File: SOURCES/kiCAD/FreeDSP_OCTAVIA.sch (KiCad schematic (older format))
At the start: 167 parts, among them IC1 TPS5430DDA, J13 Conn_01x05, J2 DC7.5V-9V IN, J4 Header_01x06, J7 Header_01x04, J8 Header_01x04, P1 Conn_02x20_Odd_Even, Q1 AO3401A, Q2 MMBT5401, Q3 2N7002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

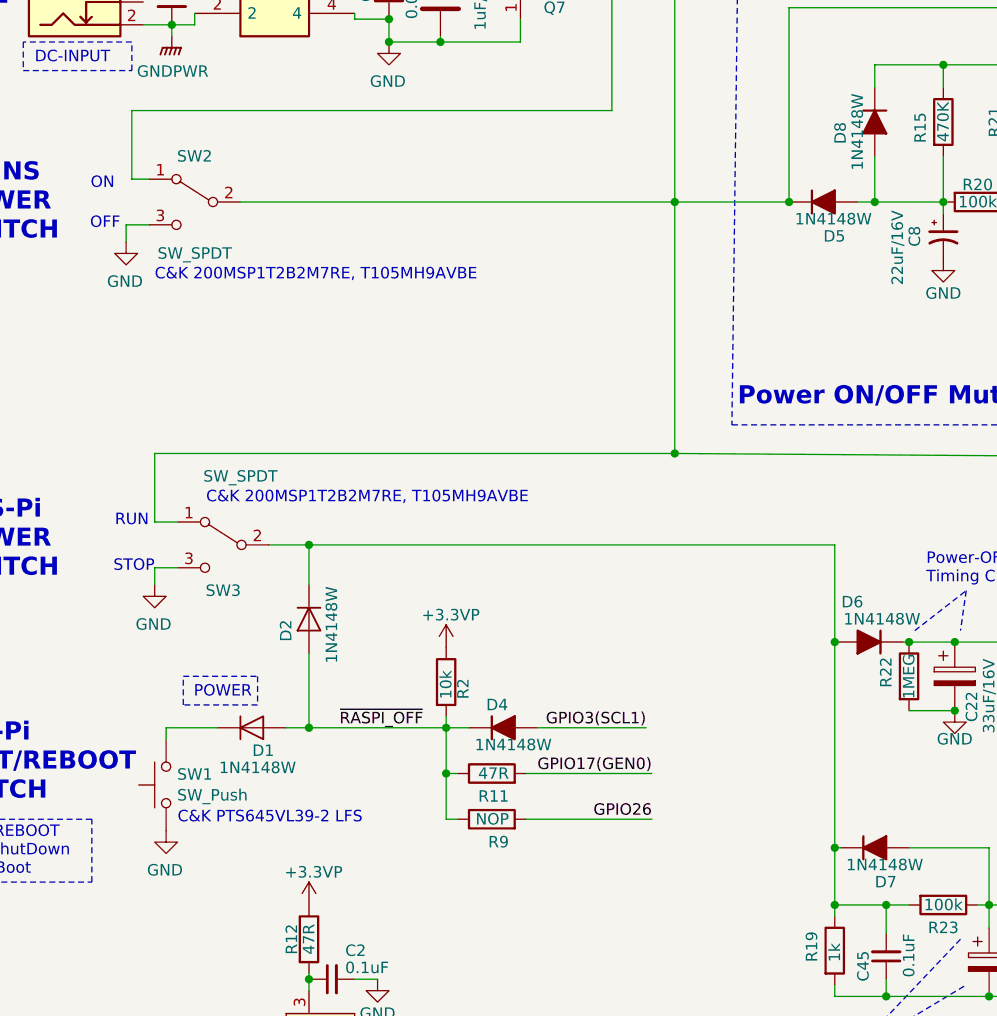
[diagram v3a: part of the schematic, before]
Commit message: A method of board type convertion had changed.
Add an AGND fill on the bottom layer. The connection path for the Standard type board had changed. No features/functions changed.
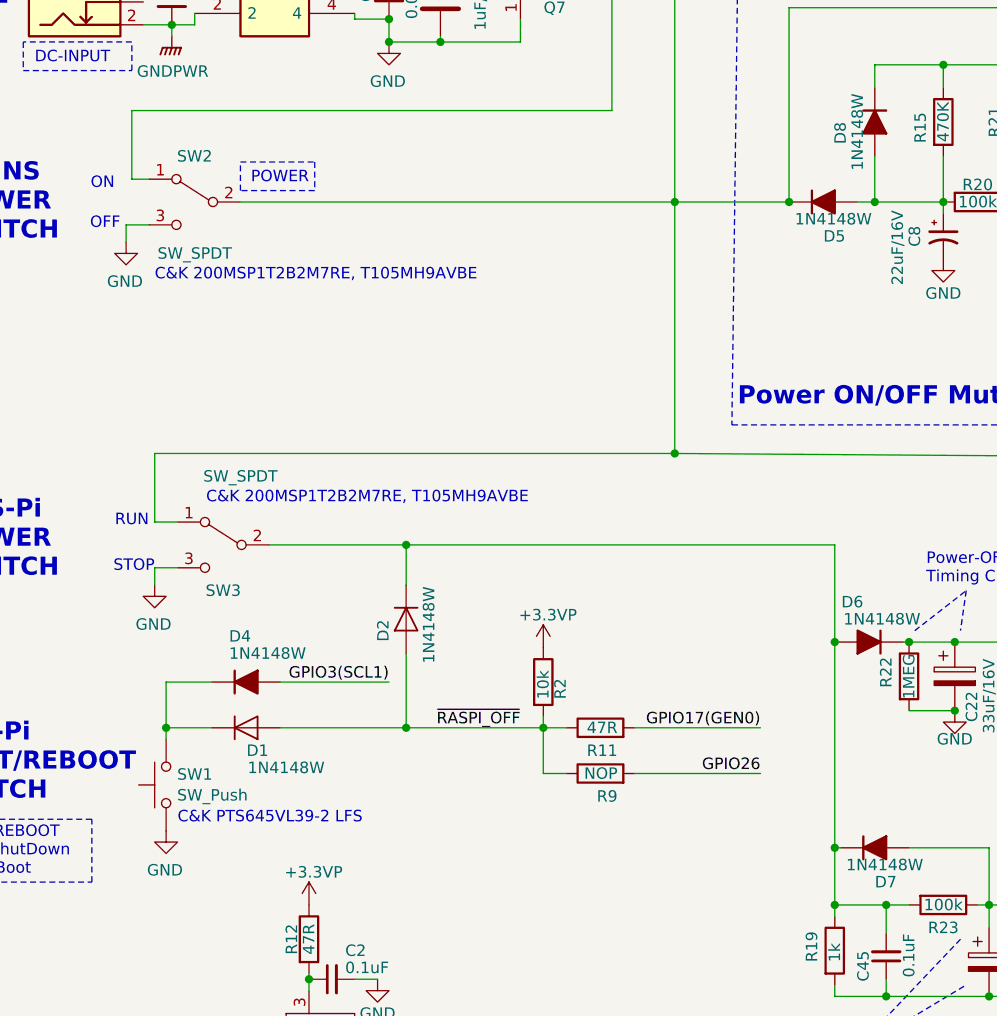
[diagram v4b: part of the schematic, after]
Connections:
- net ~RASPI_OFF: no longer D4.1 (K)
- net at D1.1 (K), SW1.2: now also D4.1 (K)
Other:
- moved on the sheet: D1, D2, D4, R11, R2, R9
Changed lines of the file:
@@
 Sheet 1 3
 Title "FreeDSP OVTAVIA Main Board"
-Date "2023-12-03"
-Rev "1.1"
+Date "2024-01-03"
+Rev "1.2"
 Comp ""
 Comment1 ""
@@
 Text Notes 2100 2375 2    50   ~ 0
 OFF
-Text Notes 2675 4425 2    50   ~ 0
+Text Notes 2925 2175 2    50   ~ 0
 POWER
 Wire Notes Line
-	2700 4325 2700 4450
+	2950 2075 2950 2200
 Wire Notes Line
-	2700 4450 2375 4450
+	2950 2200 2625 2200
 Wire Notes Line
-	2375 4450 2375 4325
+	2625 2200 2625 2075
 Wire Notes Line
-	2375 4325 2700 4325
+	2625 2075 2950 2075
 $Comp
 L Device:C_Small C?
@@
 L MW-ADAU1466BB-rescue:D-CS5368TDM-rescue-RasPiAudioHat-rescue D2
 U 1 1 5E32A9DB
-P 2925 4075
-F 0 "D2" H 2975 4175 50  0000 C CNN
-F 1 "1N4148W" H 2950 3975 50  0000 C CNN
-F 2 "Diode_SMD:D_SOD-123" H 2925 4075 50  0001 C CNN
-F 3 "" H 2925 4075 50  0001 C CNN
-F 4 "C81598 " H 2925 4075 50  0001 C CNN "JLPCB#"
-F 5 "Si Switching Diode" H 2925 4075 50  0001 C CNN "Description"
-	1    2925 4075
+P 3350 4075
+F 0 "D2" H 3400 4175 50  0000 C CNN
+F 1 "1N4148W" H 3375 3975 50  0000 C CNN
+F 2 "Diode_SMD:D_SOD-123" H 3350 4075 50  0001 C CNN
+F 3 "" H 3350 4075 50  0001 C CNN
+F 4 "C81598 " H 3350 4075 50  0001 C CNN "JLPCB#"
+F 5 "Si Switching Diode" H 3350 4075 50  0001 C CNN "Description"
+	1    3350 4075
 	0    -1   1    0
 $EndComp
-Text Label 3425 4550 2    50   ~ 0
+Text Label 3850 4550 2    50   ~ 0
 ~RASPI_OFF
 $Comp
 L MW-ADAU1466BB-rescue:D-CS5368TDM-rescue-RasPiAudioHat-rescue D1
 U 1 1 5E34C8F1
-P 2675 4550
-F 0 "D1" H 2725 4650 50  0000 C CNN
-F 1 "1N4148W" H 2700 4725 50  0000 C CNN
-F 2 "Diode_SMD:D_SOD-123" H 2675 4550 50  0001 C CNN
-F 3 "" H 2675 4550 50  0001 C CNN
-F 4 "C81598 " H 2675 4550 50  0001 C CNN "JLPCB#"
-F 5 "Si Switching Diode" H 2675 4550 50  0001 C CNN "Description"
-	1    2675 4550
+P 2650 4550
+F 0 "D1" H 2700 4650 50  0000 C CNN
+F 1 "1N4148W" H 2825 4725 50  0000 C CNN
+F 2 "Diode_SMD:D_SOD-123" H 2650 4550 50  0001 C CNN
+F 3 "" H 2650 4550 50  0001 C CNN
+F 4 "C81598 " H 2650 4550 50  0001 C CNN "JLPCB#"
+F 5 "Si Switching Diode" H 2650 4550 50  0001 C CNN "Description"
+	1    2650 4550
 	1    0    0    1
 $EndComp
@@
 RAS-Pi\nSHUT/REBOOT\nSWITCH
 Wire Wire Line
-	2300 4550 2525 4550
+	2300 4550 2500 4550
 $Comp
 L MW-ADAU1466BB-rescue:R-CS5368TDM-rescue-RasPiAudioHat-rescue R13
@@
 L Device:R R?
 U 1 1 5DF72E64
-P 3725 4750
+P 4200 4550
 AR Path="/5DEF3C17/5DF72E64" Ref="R?"  Part="1"
 AR Path="/5DF72E64" Ref="R11"  Part="1"
-F 0 "R11" V 3625 4675 50  0000 L CNN
-F 1 "47R" V 3725 4675 50  0000 L CNN
-F 2 "Resistor_SMD:R_0805_2012Metric_Pad1.20x1.40mm_HandSolder" V 3655 4750 50  0001 C CNN
-F 3 "~" H 3725 4750 50  0001 C CNN
-F 4 "C17714" H 3725 4750 50  0001 C CNN "JLPCB#"
-	1    3725 4750
+F 0 "R11" V 4100 4475 50  0000 L CNN
+F 1 "47R" V 4200 4475 50  0000 L CNN
+F 2 "Resistor_SMD:R_0805_2012Metric_Pad1.20x1.40mm_HandSolder" V 4130 4550 50  0001 C CNN
+F 3 "~" H 4200 4550 50  0001 C CNN
+F 4 "C17714" H 4200 4550 50  0001 C CNN "JLPCB#"
+	1    4200 4550
 	0    -1   -1   0
 $EndComp
-Text Label 4425 4950 2    50   ~ 0
+Text Label 4900 4750 2    50   ~ 0
 GPIO26
 Wire Wire Line
-	3875 4950 4425 4950
-Wire Wire Line
-	3525 4950 3525 4750
-Text Label 4425 4750 2    50   ~ 0
+	4350 4750 4900 4750
+Text Label 4900 4550 2    50   ~ 0
 GPIO17(GEN0)
 $Comp
 L Device:R R?
 U 1 1 5DF72E6F
-P 3725 4950
+P 4200 4750
 AR Path="/5DEF3C17/5DF72E6F" Ref="R?"  Part="1"
 AR Path="/5DF72E6F" Ref="R9"  Part="1"
-F 0 "R9" V 3625 4875 50  0000 L CNN
-F 1 "NOP" V 3725 4875 50  0000 L CNN
-F 2 "Resistor_SMD:R_0805_2012Metric_Pad1.20x1.40mm_HandSolder" V 3655 4950 50  0001 C CNN
-F 3 "~" H 3725 4950 50  0001 C CNN
-F 4 "NOP" H 3725 4950 50  0001 C CNN "JLPCB#"
-F 5 "Selectable Exclusive Mount Jumper R" H 3725 4950 50  0001 C CNN "Description"
-	1    3725 4950
+F 0 "R9" V 4100 4675 50  0000 L CNN
+F 1 "NOP" V 4200 4675 50  0000 L CNN
+F 2 "Resistor_SMD:R_0805_2012Metric_Pad1.20x1.40mm_HandSolder" V 4130 4750 50  0001 C CNN
+F 3 "~" H 4200 4750 50  0001 C CNN
+F 4 "NOP" H 4200 4750 50  0001 C CNN "JLPCB#"
+F 5 "Selectable Exclusive Mount Jumper R" H 4200 4750 50  0001 C CNN "Description"
+	1    4200 4750
 	0    -1   -1   0
 $EndComp
-Connection ~ 3525 4750
 Wire Wire Line
-	3875 4750 4425 4750
+	4350 4550 4900 4550
 $Comp
 L Device:D_ALT D?
 U 1 1 5DF72E77
-P 3775 4550
+P 2650 4350
 AR Path="/5D60B524/5DF72E77" Ref="D?"  Part="1"
 AR Path="/5DF72E77" Ref="D4"  Part="1"
 AR Path="/5DEF3C17/5DF72E77" Ref="D?"  Part="1"
-F 0 "D4" H 3700 4650 50  0000 L CNN
-F 1 "1N4148W" H 3650 4475 50  0000 L CNN
-F 2 "Diode_SMD:D_SOD-123" H 3775 4550 50  0001 C CNN
-F 3 "~" H 3775 4550 50  0001 C CNN
-F 4 "C81598 " H 3775 4550 50  0001 C CNN "JLPCB#"
-F 5 "Si Switching Diode" H 3775 4550 50  0001 C CNN "Description"
-	1    3775 4550
+F 0 "D4" H 2575 4550 50  0000 L CNN
+F 1 "1N4148W" H 2575 4475 50  0000 L CNN
+F 2 "Diode_SMD:D_SOD-123" H 2650 4350 50  0001 C CNN
+F 3 "~" H 2650 4350 50  0001 C CNN
+F 4 "C81598 " H 2650 4350 50  0001 C CNN "JLPCB#"
+F 5 "Si Switching Diode" H 2650 4350 50  0001 C CNN "Description"
+	1    2650 4350
 	1    0    0    -1
 $EndComp
 Wire Wire Line
-	3525 4550 3525 4750
+	3950 4550 3950 4750
 Wire Wire Line
-	3925 4550 4400 4550
-Text Label 4400 4550 2    50   ~ 0
+	2800 4350 3275 4350
+Text Label 3275 4350 2    50   ~ 0
 GPIO3(SCL1)
 $Comp
 L Device:R R?
 U 1 1 5DF72E80
-P 3525 4350
+P 3950 4350
 AR Path="/5DEF3C17/5DF72E80" Ref="R?"  Part="1"
 AR Path="/5DF72E80" Ref="R2"  Part="1"
-F 0 "R2" V 3600 4275 50  0000 L CNN
-F 1 "10k" V 3525 4275 50  0000 L CNN
-F 2 "Resistor_SMD:R_0805_2012Metric_Pad1.20x1.40mm_HandSolder" V 3455 4350 50  0001 C CNN
-F 3 "~" H 3525 4350 50  0001 C CNN
-F 4 "C17414" H 3525 4350 50  0001 C CNN "JLPCB#"
-	1    3525 4350
+F 0 "R2" V 4025 4275 50  0000 L CNN
+F 1 "10k" V 3950 4275 50  0000 L CNN
+F 2 "Resistor_SMD:R_0805_2012Metric_Pad1.20x1.40mm_HandSolder" V 3880 4350 50  0001 C CNN
+F 3 "~" H 3950 4350 50  0001 C CNN
+F 4 "C17414" H 3950 4350 50  0001 C CNN "JLPCB#"
+	1    3950 4350
 	1    0    0    -1
 $EndComp
 Wire Wire Line
-	3525 4500 3525 4550
-Connection ~ 3525 4550
-Wire Wire Line
-	3525 4550 3625 4550
-Wire Wire Line
-	3575 4750 3525 4750
+	3950 4500 3950 4550
+Connection ~ 3950 4550
 Wire Wire Line
-	3575 4950 3525 4950
+	3950 4550 4050 4550
 Wire Notes Line style solid
 	1975 5225 1975 4950
@@
 L power:+3.3VP #PWR09
 U 1 1 6069E068
-P 3525 4200
-F 0 "#PWR09" H 3675 4150 50  0001 C CNN
-F 1 "+3.3VP" H 3545 4343 50  0000 C CNN
-F 2 "" H 3525 4200 50  0001 C CNN
-F 3 "" H 3525 4200 50  0001 C CNN
-	1    3525 4200
+P 3950 4200
+F 0 "#PWR09" H 4100 4150 50  0001 C CNN
+F 1 "+3.3VP" H 3970 4343 50  0000 C CNN
+F 2 "" H 3950 4200 50  0001 C CNN
+F 3 "" H 3950 4200 50  0001 C CNN
+	1    3950 4200
 	1    0    0    -1
 $EndComp
@@
 $EndComp
 Wire Wire Line
-	2825 4550 2925 4550
+	2800 4550 3350 4550
 Wire Wire Line
-	2925 4225 2925 4550
-Connection ~ 2925 4550
+	3350 4225 3350 4550
+Connection ~ 3350 4550
 Wire Wire Line
-	2925 4550 3525 4550
+	3350 4550 3950 4550
 Wire Wire Line
 	8100 2950 8100 2400
@@
 SHUT\nOFF
 Wire Wire Line
-	2750 3750 2925 3750
+	2750 3750 3350 3750
 Wire Wire Line
 	6025 4500 7350 4500
@@
 Connection ~ 4525 3350
 Wire Wire Line
-	2925 3925 2925 3750
-Connection ~ 2925 3750
+	3350 3925 3350 3750
+Connection ~ 3350 3750
 Wire Wire Line
-	2925 3750 5225 3750
+	3350 3750 5225 3750
 Wire Wire Line
 	7275 2450 6950 2450
@@
 Text Notes 8050 10225 0    49   ~ 0
 RPi
+Wire Wire Line
+	2500 4350 2300 4350
+Wire Wire Line
+	2300 4350 2300 4550
+Connection ~ 2300 4550
+Wire Wire Line
+	3950 4750 4050 4750
 $EndSCHEMATC
